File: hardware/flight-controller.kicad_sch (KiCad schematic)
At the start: 107 parts, among them J1 USB_C_Receptacle_USB2.0_16P, J10 Screw_Terminal_01x02, J11 Micro_SD_Card_Det_Hirose_DM3AT, J12 Conn_01x03, J13 Conn_01x03, J14 Conn_01x03, J15 Conn_01x03, J16 Screw_Terminal_01x02, J17 Conn_01x04, J18 Screw_Terminal_01x02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

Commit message: finished board
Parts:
- added C39: 100nF, Capacitor_SMD:C_0402_1005Metric, symbol Device:C
- added SET1: SW_Push, Button_Switch_SMD:SW_Push_SPST_NO_Alps_SKRK, symbol Switch:SW_Push
- J10, J16, J18, J5, J7, J9: footprint TerminalBlock_4Ucon:TerminalBlock_4Ucon_1x02_P3.50mm_Horizontal -> TerminalBlock:TerminalBlock_MaiXu_MX126-5.0-02P_1x02_P5.00mm
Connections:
- net GND: now also C39.1, SET1.1
- net SET_BTN: now reaches U7.89 (PB3(JTDO)
- net SET_BTN: now also C39.2, SET1.2
- no-connect marks 54 -> 53
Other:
- moved on the sheet: BOOT1, BZ1, C11, R16, R28, RESET1

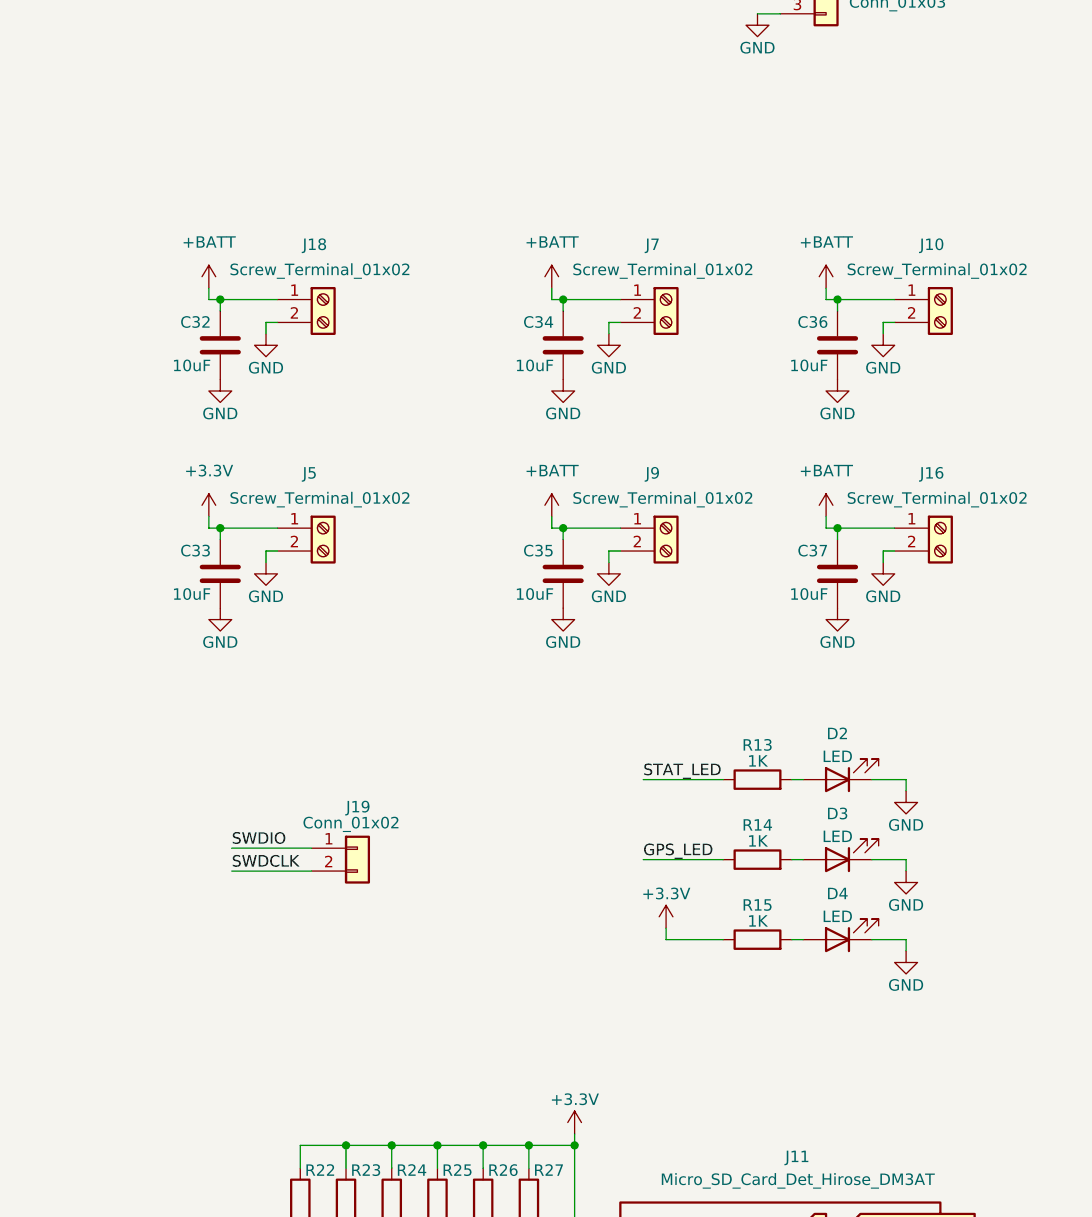
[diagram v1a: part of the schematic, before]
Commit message: added I2C pins
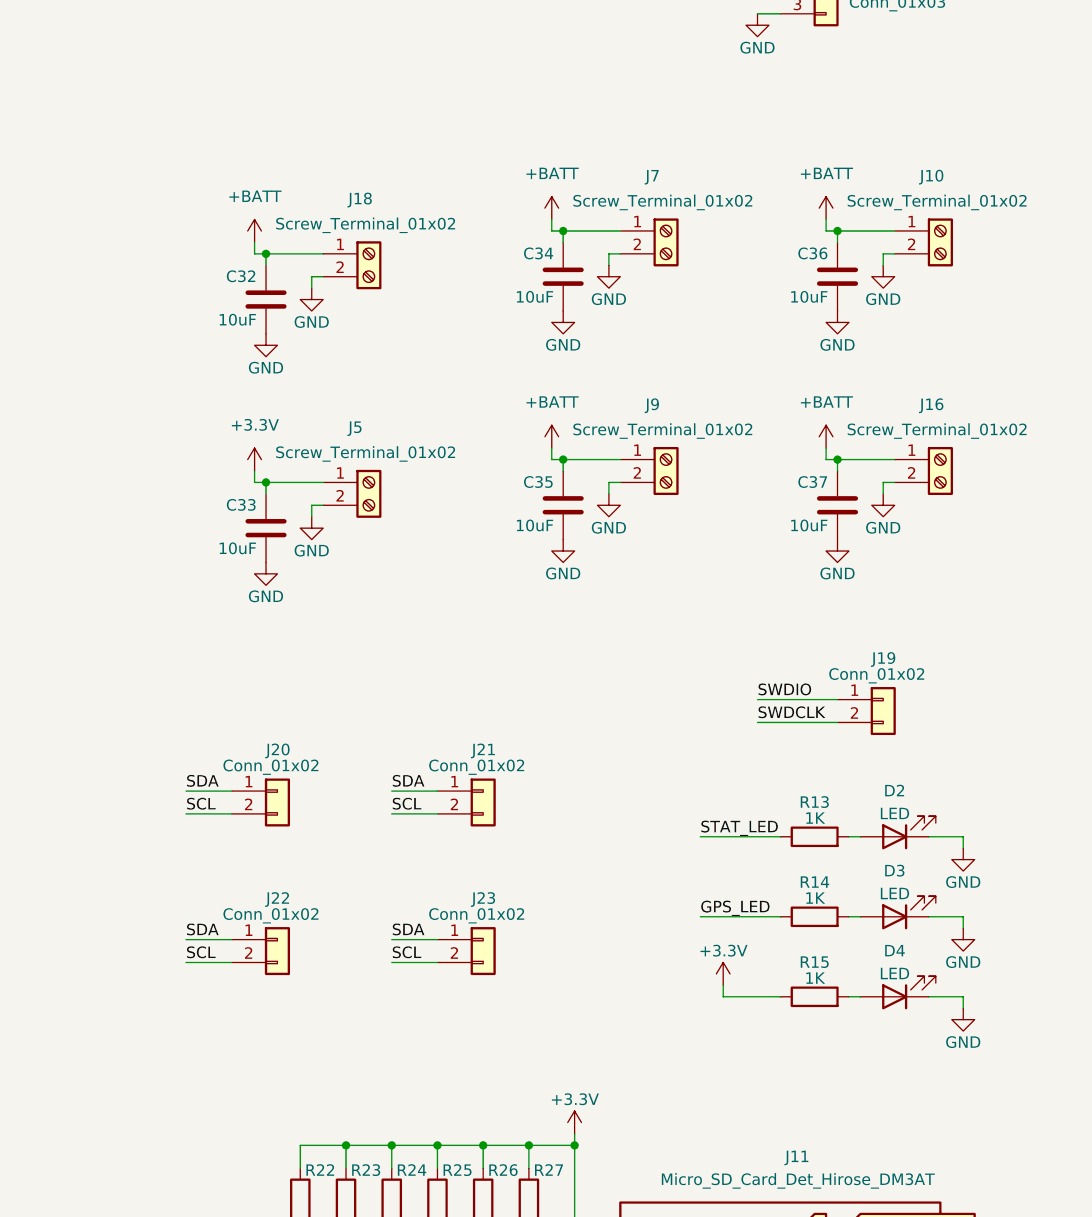
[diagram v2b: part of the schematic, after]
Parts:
- added J20, J21, J22, J23: Conn_01x02, Connector_PinHeader_2.54mm:PinHeader_1x02_P2.54mm_Vertical, symbol Connector_Generic:Conn_01x02
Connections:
- net SCL: now also J20.2 (Pin_2), J21.2 (Pin_2), J22.2 (Pin_2), J23.2 (Pin_2)
- net SDA: now also J20.1 (Pin_1), J21.1 (Pin_1), J22.1 (Pin_1), J23.1 (Pin_1)
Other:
- moved on the sheet: C32, C33, C34, C35, C36, C37, D2, D3, D4, J10, J16, J18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

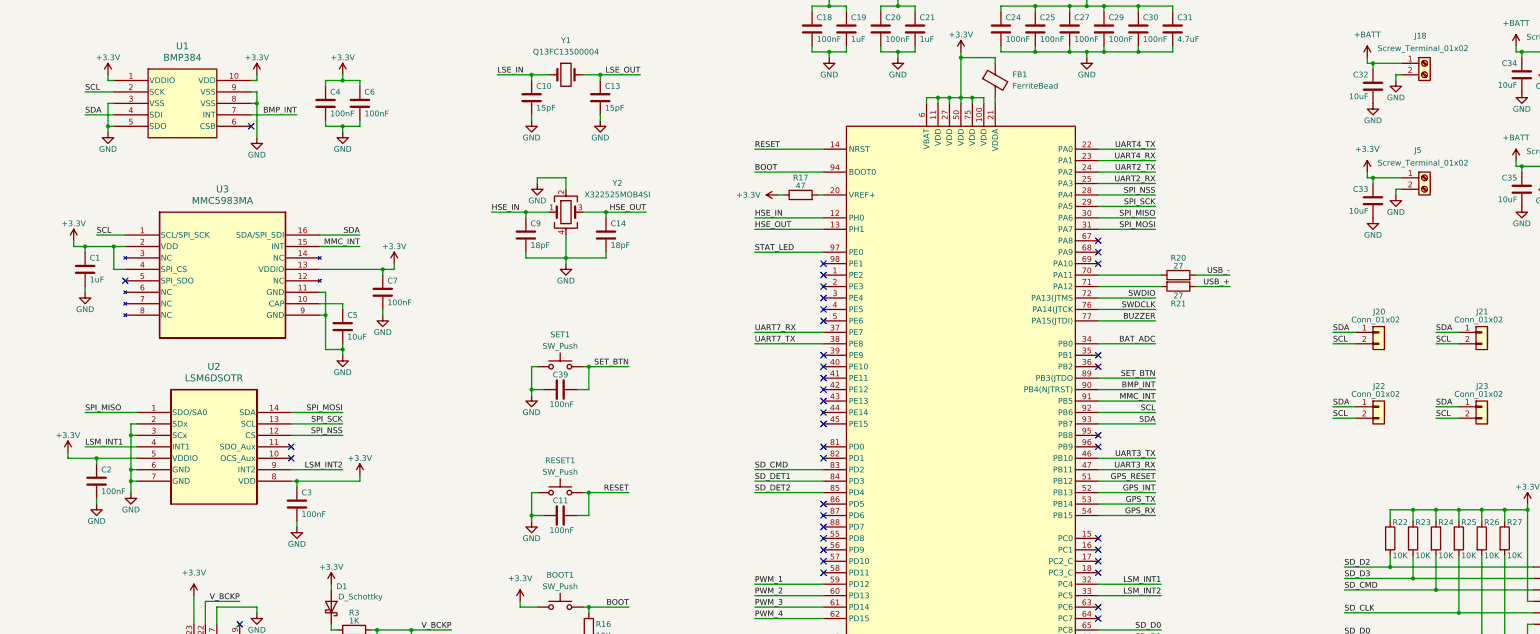
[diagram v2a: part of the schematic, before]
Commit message: added seperate I2C channel
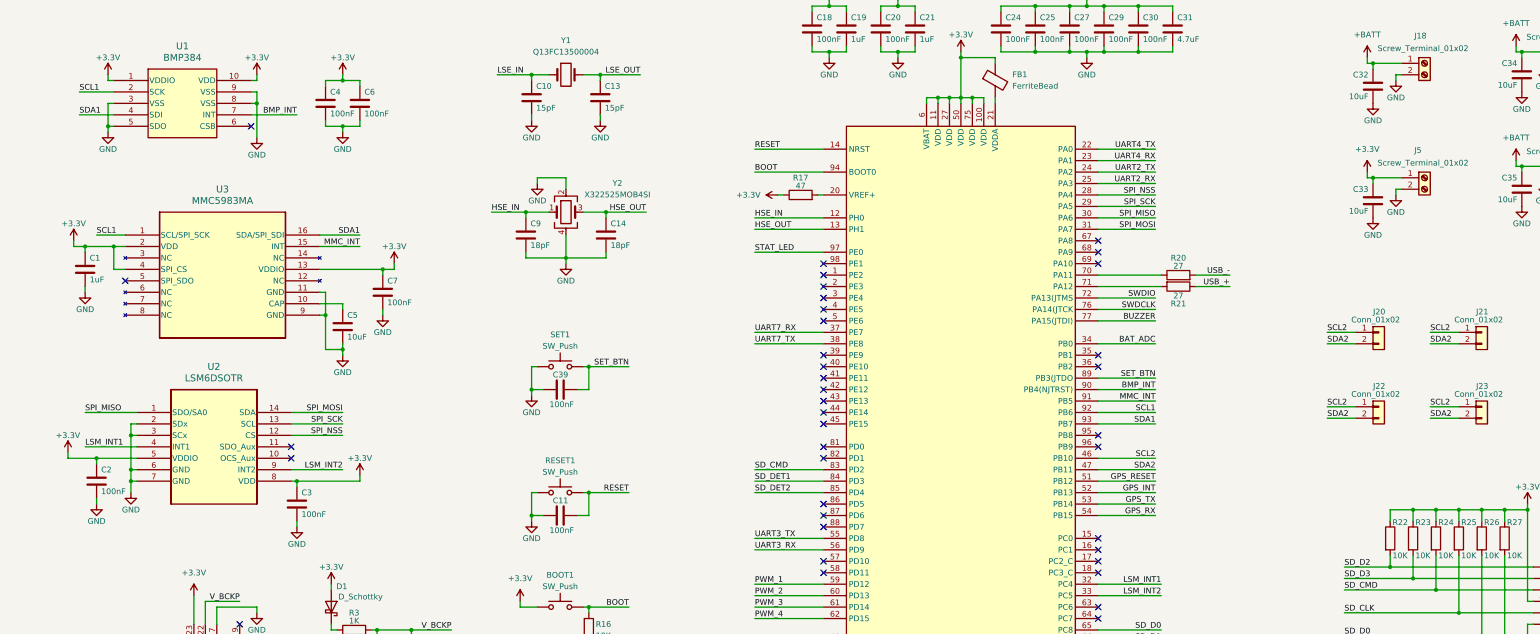
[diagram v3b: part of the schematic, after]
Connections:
- net UART3_RX: now also U7.56 (PD9); no longer U7.47 (PB11)
- net UART3_TX: now also U7.55 (PD8); no longer U7.46 (PB10)
- net SCL renamed SDA2
- net SDA2: now also U7.47 (PB11); no longer U1.2 (SCK), U3.1 (SCL/SPI_SCK), U7.92 (PB6)
- net SDA renamed SCL2
- net SCL2: now also U7.46 (PB10); no longer U1.4 (SDI), U3.16 (SDA/SPI_SDI), U7.93 (PB7)
- new net SCL1: U1.2 (SCK), U3.1 (SCL/SPI_SCK), U7.92 (PB6)
- new net SDA1: U1.4 (SDI), U3.16 (SDA/SPI_SDI), U7.93 (PB7)
- no-connect marks 53 -> 51
